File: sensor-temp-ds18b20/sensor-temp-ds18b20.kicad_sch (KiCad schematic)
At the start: 8 parts, among them J1 PWR & Sensor, J2 ESP-01S, J3 TempSensor, J4 Conn_01x03_Pin, U1 LMZM23601V3SILR

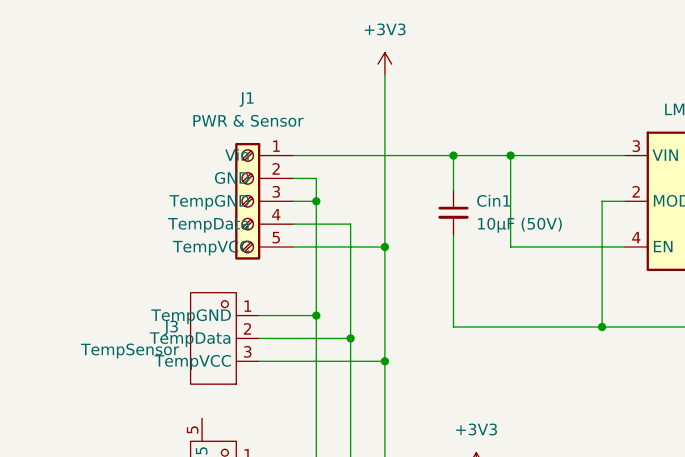
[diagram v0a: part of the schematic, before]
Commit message: Added reverse polarity protection and fixed the footprint paths
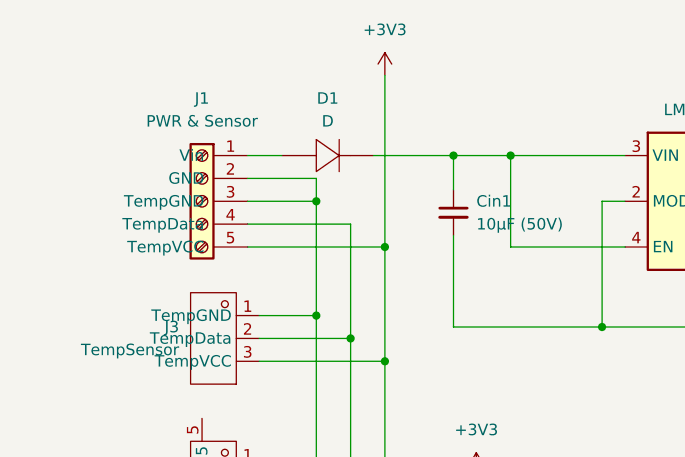
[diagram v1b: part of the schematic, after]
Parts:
- added D1: D, C5174649:SOD-323_L1.7-W1.3-LS2.5-RD, symbol C5174649:S7116-300A
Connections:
- net at Cin1.1, U1.3 (VIN), U1.4 (EN): now also D1.1 (K); no longer J1.1 (Vin)
- new net: D1.2 (A), J1.1 (Vin)
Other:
- moved on the sheet: J1
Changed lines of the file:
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@@
+	)
+	(junction
+		(at 116.84 77.47)
+		(diameter 0)
+		(color 0 0 0 0)
+	)
+	(junction
+		(at 101.6 111.76)
+		(diameter 0)
+		(color 0 0 0 0)
+	)
+	(junction
+		(at 109.22 100.33)
+		(diameter 0)
+		(color 0 0 0 0)
+	)
+	(junction
+		(at 101.6 95.25)
+		(diameter 0)
+		(color 0 0 0 0)
 	)
 	(junction
@@
 	)
 	(junction
-		(at 101.6 111.76)
-		(diameter 0)
-		(color 0 0 0 0)
-	)
-	(junction
-		(at 109.22 100.33)
-		(diameter 0)
-		(color 0 0 0 0)
-	)
-	(junction
-		(at 101.6 95.25)
-		(diameter 0)
-		(color 0 0 0 0)
-	)
-	(junction
 		(at 105.41 114.3)
 		(diameter 0)
@@
 	)
 	(junction
-		(at 116.84 77.47)
-		(diameter 0)
-		(color 0 0 0 0)
-	)
-	(junction
 		(at 101.6 82.55)
 		(diameter 0)
@@
 	(wire
 		(pts
-			(xy 99.06 80.01) (xy 101.6 80.01)
-		)
-		(stroke
-			(width 0)
-			(type default)
-		)
-	)
-	(wire
-		(pts
 			(xy 105.41 114.3) (xy 105.41 127)
 		)
@@
 	(wire
 		(pts
-			(xy 99.06 82.55) (xy 101.6 82.55)
+			(xy 93.98 80.01) (xy 101.6 80.01)
 		)
 		(stroke
@@
 	(wire
 		(pts
-			(xy 99.06 87.63) (xy 109.22 87.63)
-		)
-		(stroke
-			(width 0)
-			(type default)
-		)
-	)
-	(wire
-		(pts
 			(xy 116.84 86.36) (xy 116.84 96.52)
 		)
@@
 	(wire
 		(pts
+			(xy 109.22 87.63) (xy 109.22 100.33)
+		)
+		(stroke
+			(width 0)
+			(type default)
+		)
+	)
+	(wire
+		(pts
 			(xy 119.38 127) (xy 132.08 127)
 		)
@@
 	(wire
 		(pts
+			(xy 107.95 77.47) (xy 116.84 77.47)
+		)
+		(stroke
+			(width 0)
+			(type default)
+		)
+	)
+	(wire
+		(pts
 			(xy 152.4 113.03) (xy 152.4 127)
 		)
@@
 	(wire
 		(pts
-			(xy 99.06 85.09) (xy 105.41 85.09)
-		)
-		(stroke
-			(width 0)
-			(type default)
-		)
-	)
-	(wire
-		(pts
 			(xy 142.24 127) (xy 152.4 127)
 		)
@@
 	(wire
 		(pts
+			(xy 93.98 85.09) (xy 105.41 85.09)
+		)
+		(stroke
+			(width 0)
+			(type default)
+		)
+	)
+	(wire
+		(pts
 			(xy 101.6 95.25) (xy 101.6 111.76)
 		)
@@
 	(wire
 		(pts
+			(xy 93.98 82.55) (xy 101.6 82.55)
+		)
+		(stroke
+			(width 0)
+			(type default)
+		)
+	)
+	(wire
+		(pts
 			(xy 180.34 77.47) (xy 193.04 77.47)
 		)
@@
 	(wire
 		(pts
+			(xy 93.98 87.63) (xy 109.22 87.63)
+		)
+		(stroke
+			(width 0)
+			(type default)
+		)
+	)
+	(wire
+		(pts
 			(xy 161.29 77.47) (xy 167.64 77.47)
 		)
@@
 	(wire
 		(pts
+			(xy 93.98 77.47) (xy 97.79 77.47)
+		)
+		(stroke
+			(width 0)
+			(type default)
+		)
+	)
+	(wire
+		(pts
 			(xy 193.04 77.47) (xy 193.04 76.2)
 		)
@@
 	(wire
 		(pts
-			(xy 99.06 77.47) (xy 116.84 77.47)
-		)
-		(stroke
-			(width 0)
-			(type default)
-		)
-	)
-	(wire
-		(pts
 			(xy 95.25 111.76) (xy 101.6 111.76)
 		)
@@
 		(pts
 			(xy 101.6 82.55) (xy 101.6 80.01)
-		)
-		(stroke
-			(width 0)
-			(type default)
-		)
-	)
-	(wire
-		(pts
-			(xy 109.22 87.63) (xy 109.22 100.33)
 		)
 		(stroke
@@
 	)
 	(symbol
+		(lib_id "C5174649:S7116-300A")
+		(at 102.87 77.47 0)
+		(mirror y)
+		(unit 1)
+		(exclude_from_sim no)
+		(in_bom yes)
+		(on_board yes)
+		(dnp no)
+		(property "Reference" "D1"
+			(at 102.87 71.12 0)
+			(effects
+				(font
+					(size 1.27 1.27)
+				)
+			)
+		)
+		(property "Value" "D"
+			(at 102.87 73.66 0)
+			(effects
+				(font
+					(size 1.27 1.27)
+				)
+			)
+		)
+		(property "Footprint" "C5174649:SOD-323_L1.7-W1.3-LS2.5-RD"
+			(at 102.87 77.47 0)
+			(effects
+				(font
+					(size 1.27 1.27)
+				)
+				(hide yes)
+			)
+		)
+		(property "Datasheet" "https://atta.szlcsc.com/upload/public/pdf/source/20220916/6E626650AF012B3914EB9177AF15DFBA.pdf"
+			(at 102.87 77.47 0)
+			(effects
+				(font
+					(size 1.27 1.27)
+				)
+				(hide yes)
+			)
+		)
+		(property "Description" "Diode Configuration: Forward Voltage (Vf@If):500mV@1A Reverse Voltage (Vr): Average Rectified Current (Io):"
+			(at 102.87 77.47 0)
+			(effects
+				(font
+					(size 1.27 1.27)
+				)
+				(hide yes)
+			)
+		)
+		(property "Sim.Device" "D"
+			(at 102.87 77.47 0)
+			(effects
+				(font
+					(size 1.27 1.27)
+				)
+				(hide yes)
+			)
+		)
+		(property "Sim.Pins" "1=K 2=A"
+			(at 102.87 77.47 0)
+			(effects
+				(font
+					(size 1.27 1.27)
+				)
+				(hide yes)
+			)
+		)
+		(property "Manufacturer Part" "S7116-300A"
+			(at 102.87 77.47 0)
+			(effects
+				(font
+					(size 1.27 1.27)
+				)
+				(hide yes)
+			)
+		)
+		(property "Manufacturer" "MSKSEMI(美森科)"
+			(at 102.87 77.47 0)
+			(effects
+				(font
+					(size 1.27 1.27)
+				)
+				(hide yes)
+			)
+		)
+		(property "Supplier Part" "C5174649"
+			(at 102.87 77.47 0)
+			(effects
+				(font
+					(size 1.27 1.27)
+				)
+				(hide yes)
+			)
+		)
+		(property "Supplier" "LCSC"
+			(at 102.87 77.47 0)
+			(effects
+				(font
+					(size 1.27 1.27)
+				)
+				(hide yes)
+			)
+		)
+		(property "LCSC Part Name" "S7116-300A"
+			(at 102.87 77.47 0)
+			(effects
+				(font
+					(size 1.27 1.27)
+				)
+				(hide yes)
+			)
+		)
+		(pin "2"
+		)
+		(pin "1"
+		)
+		(instances
+			(project ""
+				(path "/9538e4ed-27e6-4c37-b989-9859dc0d49e8"
+					(reference "D1")
+					(unit 1)
+				)
+			)
+		)
+	)
+	(symbol
 		(lib_id "Device:C_Small")
 		(at 116.84 83.82 0)
@@
 	(symbol
 		(lib_id "Connector:Screw_Terminal_01x05")
-		(at 93.98 82.55 0)
+		(at 88.9 82.55 0)
 		(mirror y)
 		(unit 1)
@@
 		(fields_autoplaced yes)
 		(property "Reference" "J1"
-			(at 93.98 71.12 0)
+			(at 88.9 71.12 0)
 			(effects
 				(font
@@
 		)
 		(property "Value" "PWR & Sensor"
-			(at 93.98 73.66 0)
+			(at 88.9 73.66 0)
 			(effects
 				(font
@@
 		)
 		(property "Footprint" "TerminalBlock_MetzConnect:TerminalBlock_MetzConnect_Type086_RT03405HBLC_1x05_P3.81mm_Horizontal"
-			(at 93.98 82.55 0)
+			(at 88.9 82.55 0)
 			(effects
 				(font
@@
 		)
 		(property "Datasheet" "~"
-			(at 93.98 82.55 0)
+			(at 88.9 82.55 0)
 			(effects
 				(font
@@
 		)
 		(property "Description" ""
-			(at 93.98 82.55 0)
+			(at 88.9 82.55 0)
 			(effects
 				(font
@@
 		)
 		(property "LCSC" "C5349553"
-			(at 93.98 82.55 0)
+			(at 88.9 82.55 0)
 			(effects
 				(font
@@
 		)
 		(property "MPN" "OSTOQ053251"
-			(at 93.98 82.55 0)
-			(effects
-				(font
+			(at 88.9 82.55 0)
+			(effects
+				(font
